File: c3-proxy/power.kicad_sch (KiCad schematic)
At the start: 12 parts, among them Q2 DMP2035UQ-7, Q5 DMP2035UQ-7, Q6 31-DMN2053UQ-13CT-ND, Q7 DMP2035UQ-7, SW1 C&K PCM13SMTR, U3 LTC4412xS6, U4 LTC4412xS6

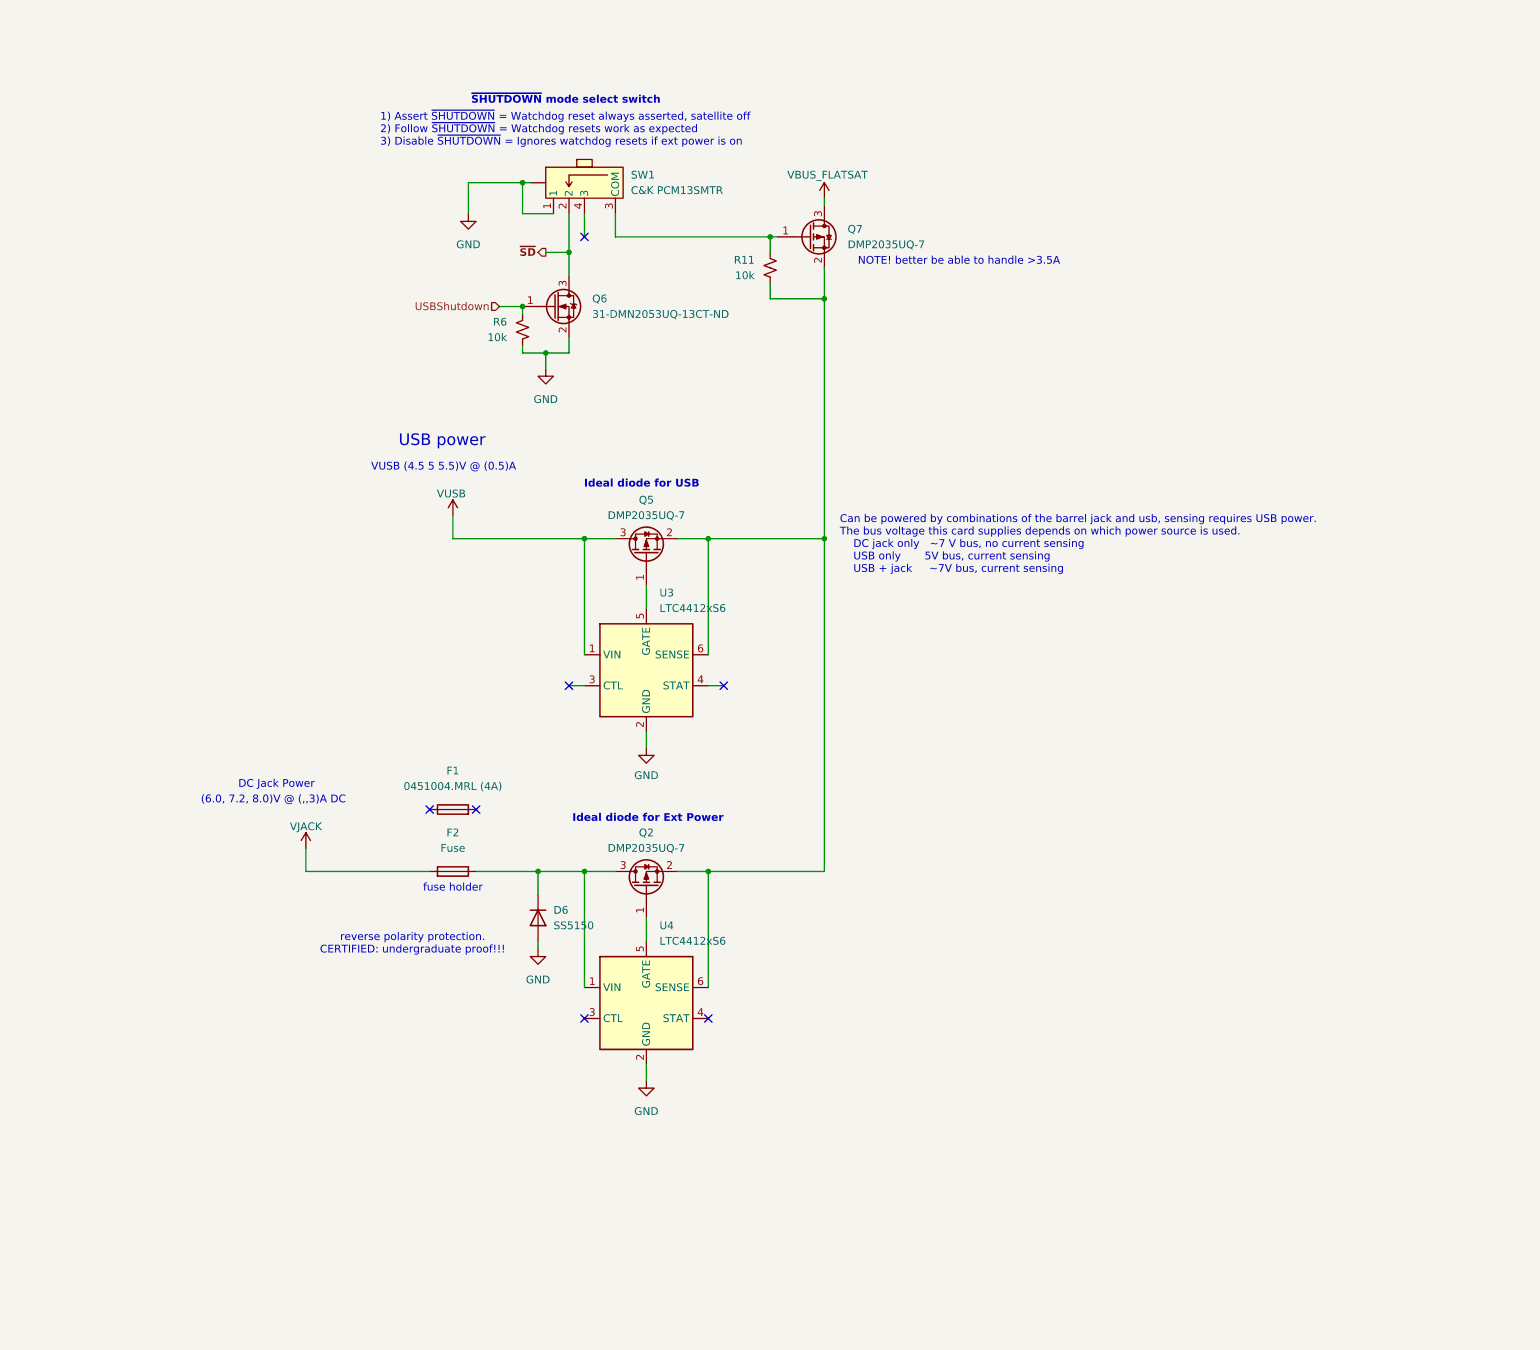
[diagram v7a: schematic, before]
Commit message: Final tweaks on v1.1.
Added more LEDs for main power, polished high power connections, DRC, ERC, etc. Added release folder.
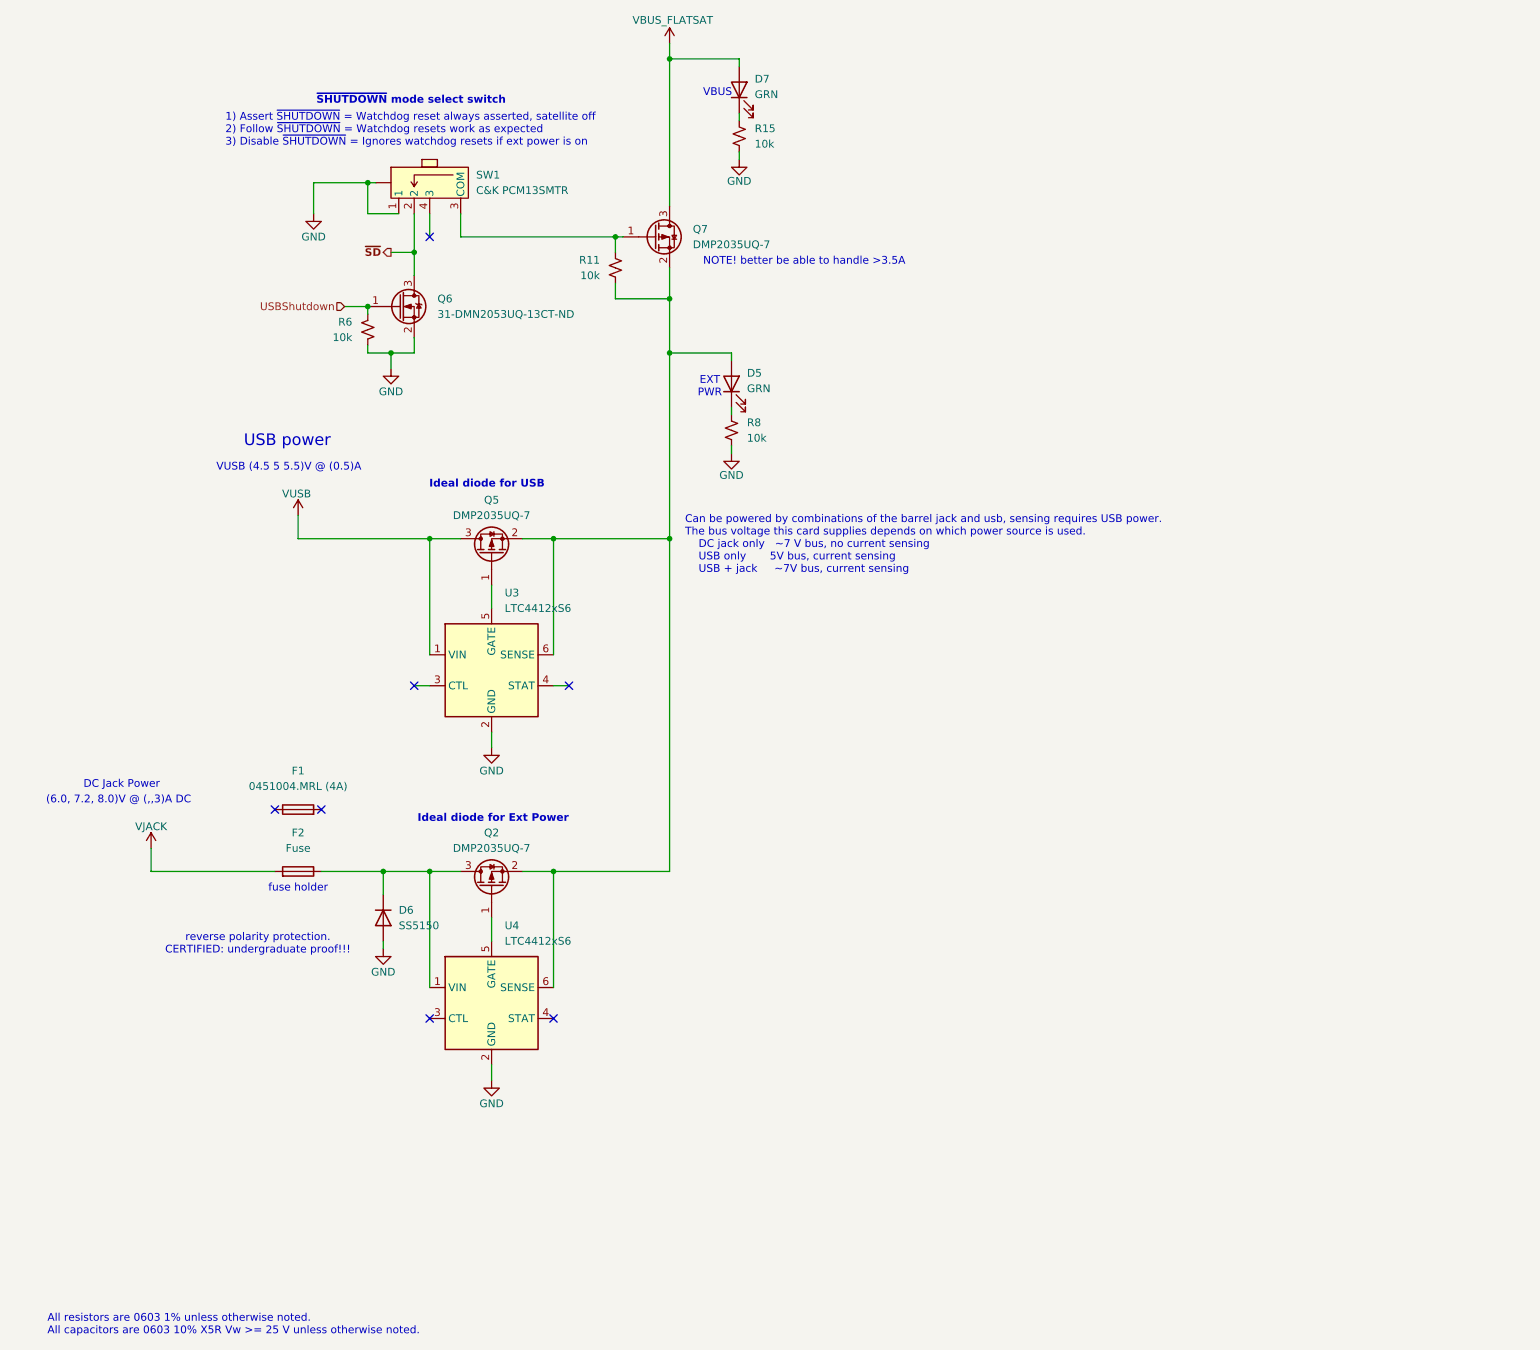
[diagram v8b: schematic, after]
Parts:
- added D5, D7: GRN, LED_SMD:LED_0603_1608Metric, symbol Device:LED
- added R15, R8: 10k, oresat-passives:0603-C-NOSILK, symbol Device:R_Small_US
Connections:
- net GND: now also R15.2, R8.2
- net VBUS_FLATSAT: now also D7.2 (A)
- net at Q2.2 (S), Q5.2 (S), Q7.2 (S)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: now also D5.2 (A)
- new net: D5.1 (K), R8.1
- new net: D7.1 (K), R15.1
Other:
- note added: "All resistors are 0603 1% unless otherwise noted. All capacitors are 0603 10% X5R Vw >= 25 V unless otherwise noted."
- note added: "EXT PWR"
- note added: "VBUS"
- title: c3-Proxy card -> c3-Proxy Board
- moved on the sheet: D6, F1, F2, Q2, Q5, Q6, Q7, R11, R6, SW1, U3, U4
